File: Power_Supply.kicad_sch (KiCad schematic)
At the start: 22 parts, among them J1 12V_Input, U1 TPS54360DDA, U2 AMS1117-3.3

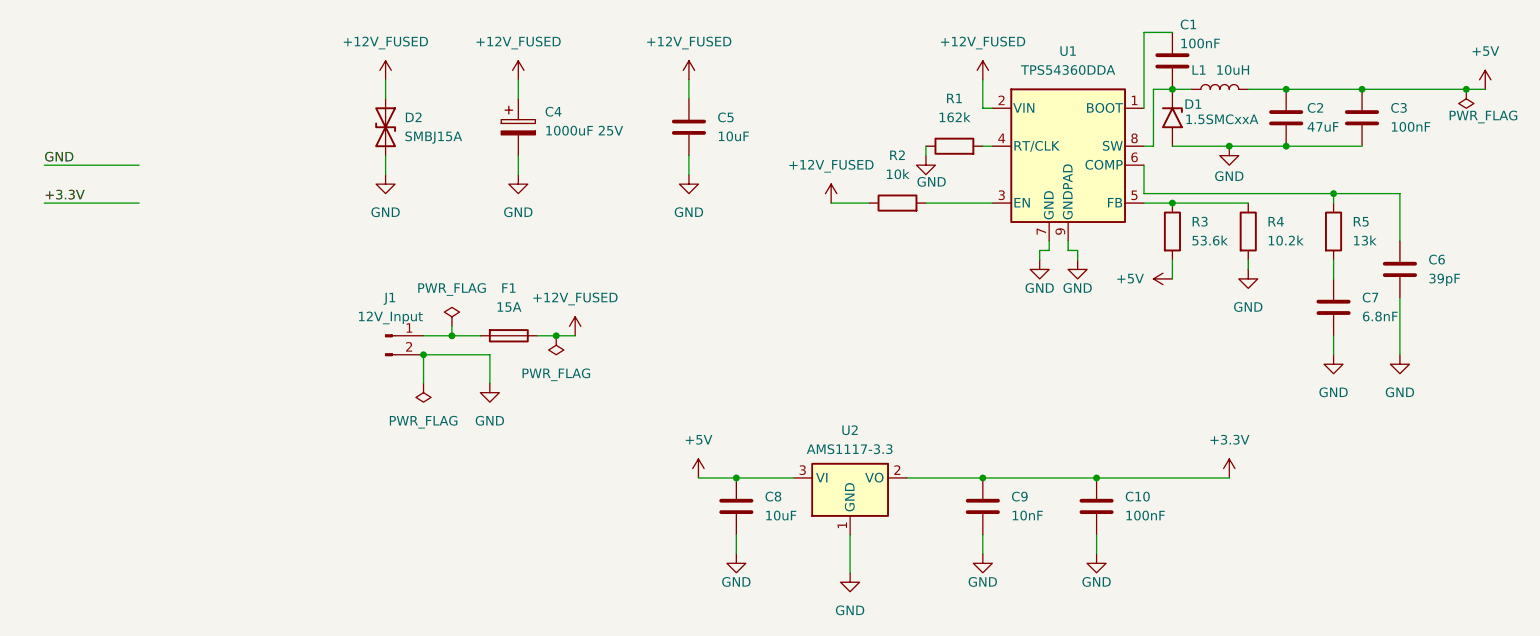
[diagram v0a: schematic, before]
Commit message: Update rail descriptions in schematic to match actual rail names.
Signed-off-by: Vincent Cadicamo <vcadicamo@icloud.com>
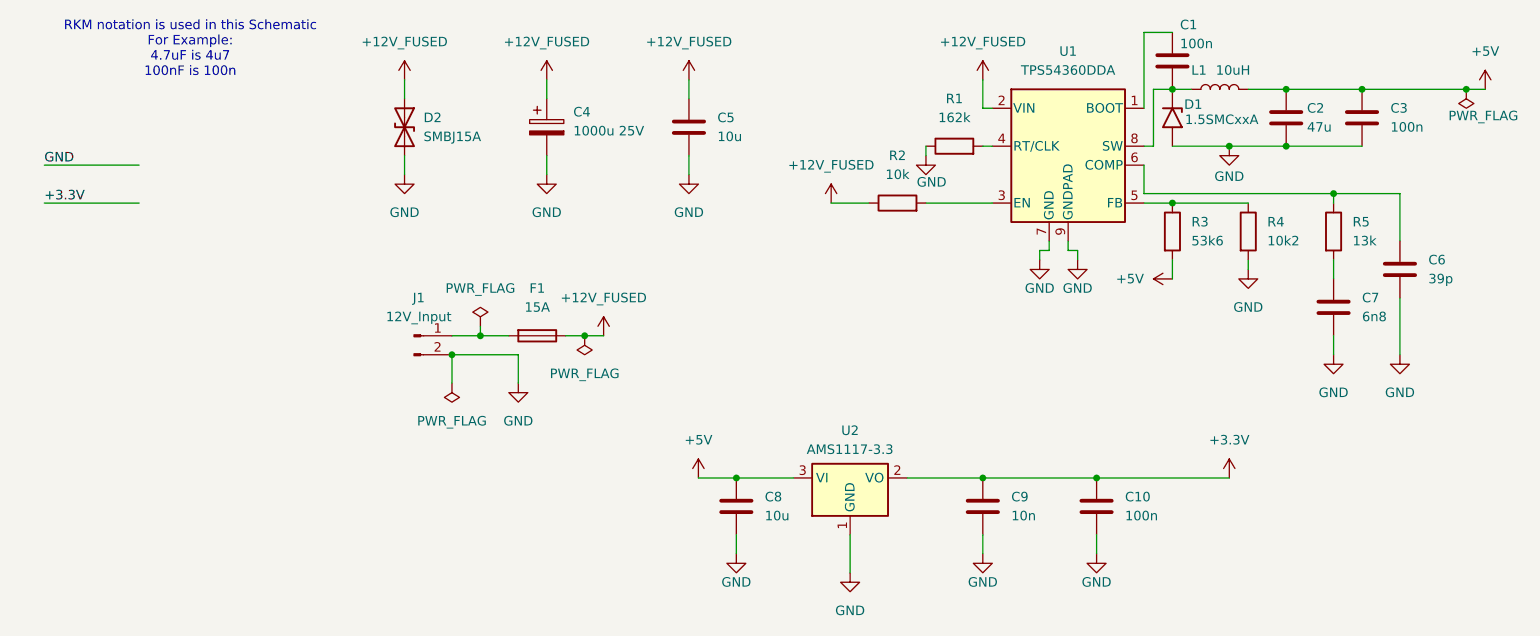
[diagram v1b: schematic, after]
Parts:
- C1, C10, C3: value 100nF -> 100n
- C2: value 47uF -> 47u
- C4: value 1000uF 25V -> 1000u 25V
- C5, C8: value 10uF -> 10u
- C6: value 39pF -> 39p
- C7: value 6.8nF -> 6n8
- C9: value 10nF -> 10n
- R3: value 53.6k -> 53k6
- R4: value 10.2k -> 10k2
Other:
- note added: "RKM notation is used in this Schematic For Example: 4.7uF is 4u7 100nF is 100n"
- moved on the sheet: C4, D2, F1, J1
